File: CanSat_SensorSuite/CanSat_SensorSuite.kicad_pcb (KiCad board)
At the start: 4 copper layers, 53 parts, among them J12 Molex_01x02, J13 Conn_02x03_Odd_Even, J2 USBC_Conn, J3 Micro_SD_Card, J4 Pin_01x02, U1 RP2350_80QFN, U2 S25FL128, U3 NCP1117_3.3, X1 ABM8-272-T3

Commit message: Example files update
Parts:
- removed BUZ1: ~, 0_Passives:BUZZER,7.5x7.5mm
- removed C19: 100nF, 0_Capacitors:C_0603_1608_DensityHigh
- removed D1: ~, 0_Passives:LED_0805_2012Metric
- removed J12: Molex_01x02, 0_Connectors:502352_0201
- removed J3: Micro_SD_Card, 0_Connectors:Molex_472192001_uSD
- removed LED1: Green, 0_Passives:LED_0603_1608Metric
- removed LED2: Red, 0_Passives:LED_0603_1608Metric
- removed R10, R9: 4k7R, 0_Resistors:R_0603_1608_DensityHigh
- removed R7, R8: ?220R?, 0_Resistors:R_0603_1608_DensityHigh
- moved C5 15.0 mm to (121.5, 90.4)
- moved C6 15.0 mm to (126.8, 95.5)
- moved C1 15.0 mm to (134.8, 81.7)
- moved C10 15.0 mm to (137.0, 83.9)
- moved C11 15.0 mm to (128.1, 79.0)
- moved C12 15.0 mm to (124.5, 81.5)
- moved C13 15.0 mm to (120.6, 88.0)
- moved C14 15.0 mm to (137.5, 87.7)
- moved C15 15.0 mm to (130.9, 96.5)
- moved C16 15.0 mm to (128.1, 98.6)
- moved C17 15.0 mm to (131.1, 98.6)
- moved C18 15.0 mm to (132.4, 72.4)
- moved C2 15.0 mm to (132.5, 82.1)
- moved C20 15.0 mm to (170.3, 61.7)
- moved C21 15.0 mm to (170.3, 64.1)
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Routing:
- net /CCT Board Schematic/MCU & Peripherals/STATUS_BUZZER-: track 8.23 -> 0.00 mm
- net /CCT Board Schematic/MCU & Peripherals/STATUS_BUZZER+: track 6.72 -> 0.00 mm
- net /CCT Board Schematic/MCU & Peripherals/STATUS_LED_R: track 4.68 -> 0.00 mm
- net +3V3: track 40.2 -> 37.6 mm, vias 5 -> 4
- net /CCT Board Schematic/MCU & Peripherals/STATUS_LED_G: track 2.34 -> 0.00 mm
- net Net-(LED2-K): track 1.56 -> 0.00 mm
- net Net-(LED1-K): track 1.56 -> 0.00 mm
- net GND: vias 29 -> 28
- added copper zone on In2.Cu, net +3V3
- added copper zone on B.Cu, net GND
- added copper zone on In1.Cu, net GND
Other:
- board outline added: 100 x 80 mm
- board text removed: "???mm"
- board text removed: "???mm (?oz)"
- board text removed: "B.Mask"
- board text removed: "B.Paste"
- board text removed: "B.Silkscreen"
- board text removed: "Copper"
- board text removed: "Core"
- board text removed: "Dielectric"
- board text removed: "Dielectric Material"
- board text removed: "F.Mask"
- board text removed: "F.Paste"
- board text removed: "F.Silkscreen"
- board text removed: "FABRICATION NOTES (UNLESS OTHERWISE SPECIFIED) 1) OUTLINE DEFINED IN SEPARATE GERBER FILE WITH {dblquote}Edge_Cuts.GBR{dblquote} SUFFIX. DIMENSIONS OF CIRCUMSIZED RECTANGLE SHOWN ON THIS DWG FOR REF ONLY. 2) SEE SEPARATE DRILL FILES WITH {dblquote}.DRL{dblquote} SUFFIX FOR HOLE LOCATIONS. SELECTED HOLE LOCATIONS SHOWN ON THIS DWG FOR REF ONLY. 3) IMPEDANCE CONTROL REQUIRED. Microstrip 100-Ohm Dif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"
- board text removed: "FR-4"
- board text removed: "GBR"
- board text removed: "Gerber"
- board text removed: "Internal Plane"
- board text removed: "L1 (Sig, PWR)"
- board text removed: "L2 (GND)"
- board text removed: "L3 (Sig, PWR)"
- board text removed: "L4 (Sig, PWR)"
- board text removed: "L5 (GND)"
- board text removed: "L6 (Sig, PWR)"
- board text removed: "Layer"
- board text removed: "Layer Stack Legend"
- board text removed: "Legend"
- board text removed: "Material"
- board text removed: "Note: external layer thicknesses are specified after plating."
- board text removed: "Paste Mask"
- board text removed: "Prepreg"
- board text removed: "Signal"
- board text removed: "Solder Mask"
- board text removed: "Solder Resist"
- board text removed: "Thickness"
- board text removed: "Total thickness: 1.62mm"

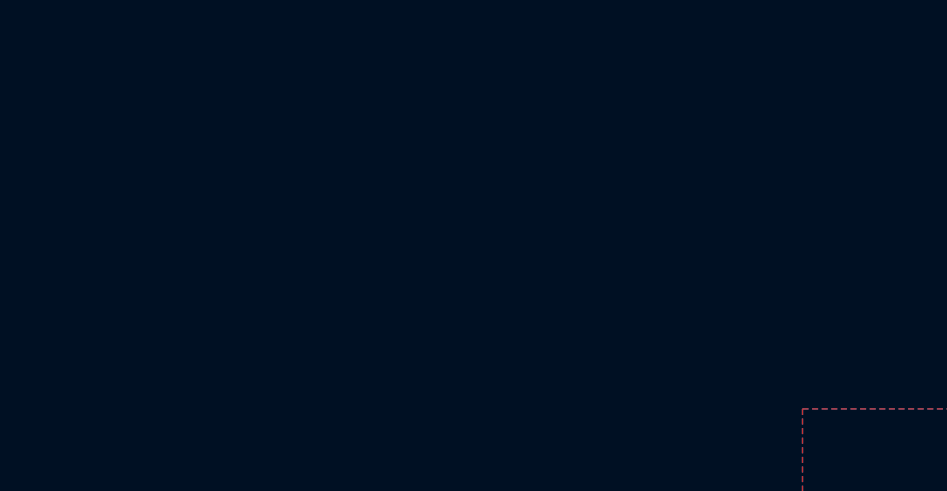
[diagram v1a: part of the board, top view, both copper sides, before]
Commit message: Minor schematic changes
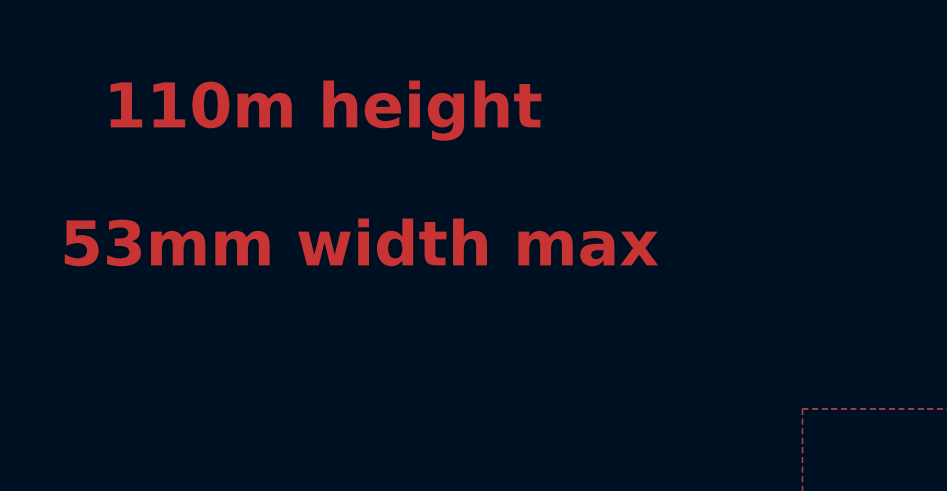
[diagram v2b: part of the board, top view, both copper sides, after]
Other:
- board text added: "110m height"
- board text added: "53mm width max"
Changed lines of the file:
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@@
 		(layer "User.9")
+	)
+	(gr_text "110m height\n"
+		(at 74.2 38.3 0)
+		(layer "F.Cu")
+		(effects
+			(font
+				(size 1.5 1.5)
+				(thickness 0.3)
+				(bold yes)
+			)
+			(justify left bottom)
+		)
+	)
+	(gr_text "53mm width max\n"
+		(at 72.75 42.9 0)
+		(layer "F.Cu")
+		(effects
+			(font
+				(size 1.5 1.5)
+				(thickness 0.3)
+				(bold yes)
+			)
+			(justify left bottom)
+		)
 	)
 	(gr_text "Top View"

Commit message: Major sensor suite board changes, start of PCB layout
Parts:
- removed J13: Conn_02x03_Odd_Even, 0_Connectors:PinHeader_2x03_P1.27mm_Vertical
- added BUZ1: ~, 0_Passives:BUZZER,5x5mm, F.Cu at (175.0, 99.3)
- added C101: 100nF, 0_Capacitors:C_0603_1608_DensityHigh, F.Cu at (170.8, 121.7)
- added C102: 100nF, 0_Capacitors:C_0603_1608_DensityHigh, F.Cu at (165.1, 123.0)
- added C103: 100nF, 0_Capacitors:C_0603_1608_DensityHigh, F.Cu at (148.1, 123.4)
- added C19: 100nF, 0_Capacitors:C_0603_1608_DensityHigh, F.Cu at (139.0, 100.3)
- added C201: 100nF, 0_Capacitors:C_0603_1608_DensityHigh, F.Cu at (155.7, 104.6)
- added C202: 100nF, 0_Capacitors:C_0603_1608_DensityHigh, F.Cu at (151.6, 116.1)
- added C24: 10uF, 0_Capacitors:C_0603_1608_DensityHigh, F.Cu at (153.4, 75.4)
- added C25: 10uF, 0_Capacitors:C_0603_1608_DensityHigh, F.Cu at (151.2, 75.4)
- added D1: ~, 0_Passives:D_SOD-323, F.Cu at (175.2, 94.7)
- added F3: Fuse, 0_Power:Fuse_1210_3225Metric, F.Cu at (162.6, 68.6)
- added FID301: Fiducial Marker, 0_Mechanical:Fiducial_1mm_Mask2mm, F.Cu at (134.3, 134.6)
- added FID302: Fiducial Marker, 0_Mechanical:Fiducial_1mm_Mask2mm, F.Cu at (175.3, 133.0)
- added FID303: Fiducial Marker, 0_Mechanical:Fiducial_1mm_Mask2mm, F.Cu at (142.1, 39.3)
- added G***: LOGO, SUSF_Footprint_Lib:SUSF_LOGO_BIG, F.Cu at (154.4, 134.8)
- added J1: Micro_SD_Card, 0_Connectors:Molex_472192001_uSD, F.Cu at (137.7, 109.8)
- added J101: SPS30, 0_Connectors:JST-S5B-ZR, F.Cu at (174.8, 127.6)
- added J104: Molex_01x02, 0_Connectors:502352_0201, F.Cu at (173.9, 112.0)
- added J3: USBC_Conn, 0_Connectors:USB4105_GCT, F.Cu at (155.0, 39.3)
- added J401: Molex_01x02, 0_Connectors:502352_0201, F.Cu at (136.1, 126.9)
- added J402: Conn_02x03, 0_Connectors:PinHeader_2x03_P1.27mm_Vertical, F.Cu at (167.5, 91.3)
- added LED1: Green, 0_Passives:LED_0603_1608Metric, F.Cu at (176.7, 88.2)
- added LED2: Red, 0_Passives:LED_0603_1608Metric, F.Cu at (176.7, 90.8)
- added LED3: Red, 0_Passives:LED_0603_1608Metric, F.Cu at (143.0, 47.6)
- added LED4: Red, 0_Passives:LED_0603_1608Metric, F.Cu at (151.9, 59.4)
- added LED5: Red, 0_Passives:LED_0603_1608Metric, F.Cu at (148.7, 75.7)
- added MH301: M3_MountingHole_Pad, 0_Mechanical:MountingHole_3.2mm_M3_Pad_Via, F.Cu at (135.0, 140.0)
- added MH302: M3_MountingHole_Pad, 0_Mechanical:MountingHole_3.2mm_M3_Pad_Via, F.Cu at (175.0, 140.0)
- added MH303: M3_MountingHole_Pad, 0_Mechanical:MountingHole_3.2mm_M3_Pad_Via, F.Cu at (135.0, 40.0)
- added MH304: M3_MountingHole_Pad, 0_Mechanical:MountingHole_3.2mm_M3_Pad_Via, F.Cu at (175.0, 40.0)
- added R10: 4.7kR, 0_Resistors:R_0603_1608_DensityHigh, F.Cu at (152.9, 100.9)
- added R14: 51R, 0_Resistors:R_0603_1608_DensityHigh, F.Cu at (152.1, 63.0)
- added R15: ???R, 0_Resistors:R_0603_1608_DensityHigh, F.Cu at (159.9, 75.2)
- added R16: ???R, 0_Resistors:R_0603_1608_DensityHigh, F.Cu at (157.8, 75.2)
- added R17: 51R, 0_Resistors:R_0603_1608_DensityHigh, F.Cu at (155.6, 75.2)
- added R18: 470kR, 0_Resistors:R_0603_1608_DensityHigh, F.Cu at (162.8, 76.3)
- added R19: 390kR, 0_Resistors:R_0603_1608_DensityHigh, F.Cu at (162.8, 78.5)
- added R7: 51R, 0_Resistors:R_0603_1608_DensityHigh, F.Cu at (173.7, 88.4)
- added R8: 51R, 0_Resistors:R_0603_1608_DensityHigh, F.Cu at (173.7, 90.5)
- added R9: 4.7kR, 0_Resistors:R_0603_1608_DensityHigh, F.Cu at (152.9, 98.8)
- added S1: SPST_1101M2S3AQE2, 0_Power:1101M2S3AQE2, F.Cu at (166.9, 69.2)
- added U102: ZMOD4410AI1R, 0_Sensors:ZMOD4410AI1R, F.Cu at (165.3, 127.0)
- added U103: STC31-C-R3, 0_Sensors:STC31-C-R3, F.Cu at (147.4, 128.6)
- added U201: MS560702BA03-50, 0_Sensors:MS5607-02BA03, F.Cu at (155.1, 107.3)
- added U202: LSM6DSOQTR, 0_Sensors:LSM6DSOQTR, F.Cu at (154.7, 115.9)
- added U4: NCP1117_3.3, 0_Power:SOT-223-3_TabPin2, F.Cu at (157.3, 58.8)
- added U5: MIC29302AWD, 0_Power:MIC29302AWD, F.Cu at (157.0, 69.0)
- C20, C21: value DNP -> 10nF
- F1, F2: footprint 0_Passives:Fuse_2512_6332Metric -> 0_Power:Fuse_1210_3225Metric
- J2: value USBC_Conn -> Pin_01x02; footprint 0_Connectors:USB4105_GCT -> 0_Connectors:PinHeader_1x02_P2.54mm_Vertical
- J4: value Pin_01x02 -> XT30_THT_H; footprint 0_Connectors:PinHeader_1x02_P2.54mm_Vertical -> 0_Connectors:XT30_THT_H
- L1: value 1uH -> 3.3uH
- R1, R2, R6: footprint 0_Resistors:R_0402_1005_DensityHigh -> 0_Resistors:R_0603_1608_DensityHigh
- R13: value 0R -> 51R; footprint 0_Resistors:R_0805_2012_DensityHigh -> 0_Resistors:R_0603_1608_DensityHigh
- R4: value 10kR -> 1kR; footprint 0_Resistors:R_0603_1608_DensityHigh -> 0_Resistors:R_0402_1005_DensityMedium
- R5: value 1kR -> 10kR
- U1: value RP2350_80QFN -> RP2350B
- moved J2 46.5 mm to (134.8, 94.3), turned to 90 degrees
- moved R4 40.9 mm to (160.9, 95.7), turned to -45 degrees
- moved X1 35.6 mm to (165.0, 99.8), turned to 45 degrees
- moved U3 35.2 mm to (136.2, 54.3)
- moved F1 33.6 mm to (138.6, 47.2)
- moved C16 33.2 mm to (161.3, 98.4), turned to -135 degrees
- moved C17 32.3 mm to (163.3, 96.4), turned to 45 degrees
- moved J4 32.0 mm to (166.8, 54.7), turned to -90 degrees
- moved C15 32.0 mm to (160.3, 84.0), turned to -135 degrees
- moved C6 31.5 mm to (158.3, 97.1), turned to -45 degrees
- moved C7 31.1 mm to (159.2, 96.2), turned to -45 degrees
- moved R13 30.5 mm to (146.6, 48.0), turned to 180 degrees
- moved C21 30.4 mm to (143.3, 50.0), turned to 180 degrees
- moved C5 30.1 mm to (150.8, 97.3), turned to -135 degrees
- moved C13 29.1 mm to (148.6, 96.2), turned to 45 degrees
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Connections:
- net /CCT Board Schematic/MCU & Peripherals/QSPI_SCLK renamed /Sensor Board Schematic/MCU & Peripherals/QSPI_SCLK
- net /CCT Board Schematic/MCU & Peripherals/QSPI_SD0 renamed /Sensor Board Schematic/MCU & Peripherals/QSPI_SD0
- net /CCT Board Schematic/MCU & Peripherals/QSPI_SD1 renamed /Sensor Board Schematic/MCU & Peripherals/QSPI_SD1
- net /CCT Board Schematic/MCU & Peripherals/QSPI_SD2 renamed /Sensor Board Schematic/MCU & Peripherals/QSPI_SD2
- net /CCT Board Schematic/MCU & Peripherals/QSPI_SD3 renamed /Sensor Board Schematic/MCU & Peripherals/QSPI_SD3
- net /CCT Board Schematic/MCU & Peripherals/USB_DM renamed /Sensor Board Schematic/MCU & Peripherals/USB_DM
- net /CCT Board Schematic/MCU & Peripherals/USB_DP renamed /Sensor Board Schematic/MCU & Peripherals/USB_DP
- net /CCT Board Schematic/MCU & Peripherals/VREG_AVDD renamed /Sensor Board Schematic/MCU & Peripherals/VREG_AVDD
- net /CCT Board Schematic/MCU & Peripherals/VREG_LX renamed /Sensor Board Schematic/MCU & Peripherals/VREG_LX
- net /CCT Board Schematic/MCU & Peripherals/XIN renamed /Sensor Board Schematic/MCU & Peripherals/XIN
- C21 pad 1: GND -> +3V3
- C21 pad 2: VBUS_F -> GND
- C22 pad 2: VBUS_F -> VREG
- C23 pad 1: Net-(U3-VO) -> +3V3
- D2 pad 1: /CCT Board Schematic/USBC/D- -> /Sensor Board Schematic/USBC & Battery Supply/D-
- D2 pad 3: /CCT Board Schematic/USBC/D+ -> /Sensor Board Schematic/USBC & Battery Supply/D+
- D2 pad 4: /CCT Board Schematic/USBC/USB_D+ -> /Sensor Board Schematic/MCU & Peripherals/USB_D+
- D2 pad 6: /CCT Board Schematic/USBC/USB_D- -> /Sensor Board Schematic/MCU & Peripherals/USB_D-
- F1 pad 2: /CCT Board Schematic/USBC/VBUS_PF -> /Sensor Board Schematic/USBC & Battery Supply/VBUS_PF
- F2 pad 1: +3V3 -> /Sensor Board Schematic/USBC & Battery Supply/BAT_CONN_OUT
- F2 pad 2: Net-(U3-VO) -> VBUS
- J4 pad 1: /CCT Board Schematic/MCU & Peripherals/~{USB_BOOT} -> /Sensor Board Schematic/USBC & Battery Supply/BAT_CONN_IN
- R1 pad 1: /CCT Board Schematic/MCU & Peripherals/USB_D+ -> /Sensor Board Schematic/MCU & Peripherals/USB_D+
- R11 pad 2: /CCT Board Schematic/USBC/CC2 -> /Sensor Board Schematic/USBC & Battery Supply/CC2
- R12 pad 1: /CCT Board Schematic/USBC/CC1 -> /Sensor Board Schematic/USBC & Battery Supply/CC1
- R13 pad 1: VBUS -> GND
- R13 pad 2: VBUS_F -> Net-(LED3-K)
- R2 pad 1: /CCT Board Schematic/MCU & Peripherals/USB_D- -> /Sensor Board Schematic/MCU & Peripherals/USB_D-
- R4 pad 1: /CCT Board Schematic/MCU & Peripherals/QSPI_CS -> /Sensor Board Schematic/MCU & Peripherals/XOUT
- R4 pad 2: +3V3 -> Net-(C17-Pad1)
- R5 pad 1: /CCT Board Schematic/MCU & Peripherals/QSPI_CS -> /Sensor Board Schematic/MCU & Peripherals/QSPI_CS
- R5 pad 2: /CCT Board Schematic/MCU & Peripherals/~{USB_BOOT} -> +3V3
- R6 pad 1: /CCT Board Schematic/MCU & Peripherals/XOUT -> /Sensor Board Schematic/MCU & Peripherals/QSPI_CS
- R6 pad 2: Net-(C17-Pad1) -> /Sensor Board Schematic/MCU & Peripherals/~{USB_BOOT}
- U1 pad 1: /CCT Board Schematic/MCU & Peripherals/FIRE_SIGNAL -> /Sensor Board Schematic/MCU & Peripherals/SD_DAT1
- U1 pad 11: /CCT Board Schematic/MCU & Peripherals/Servo2_PWM -> unconnected-(U1A-GPIO12-Pad11)
- U1 pad 12: /CCT Board Schematic/MCU & Peripherals/SD_DAT1 -> unconnected-(U1A-GPIO13-Pad12)
- U1 pad 13: /CCT Board Schematic/MCU & Peripherals/Servo3_PWM -> unconnected-(U1A-GPIO14-Pad13)
- U1 pad 14: /CCT Board Schematic/MCU & Peripherals/SD_DAT0 -> unconnected-(U1A-GPIO15-Pad14)
- U1 pad 16: /CCT Board Schematic/MCU & Peripherals/SD_CLK -> unconnected-(U1A-GPIO16-Pad16)
- U1 pad 17: /CCT Board Schematic/MCU & Peripherals/SD_CMD -> unconnected-(U1A-GPIO17-Pad17)
- U1 pad 18: /CCT Board Schematic/MCU & Peripherals/SD_DAT3 -> unconnected-(U1A-GPIO18-Pad18)
- U1 pad 19: /CCT Board Schematic/MCU & Peripherals/SD_DAT2 -> unconnected-(U1A-GPIO19-Pad19)
- U1 pad 2: /CCT Board Schematic/MCU & Peripherals/ARM_SIGNAL -> /Sensor Board Schematic/MCU & Peripherals/SD_DAT0
- U1 pad 20: /CCT Board Schematic/MCU & Peripherals/I2C_SDA -> /Sensor Board Schematic/AtmoSensors/I2C_SDA
- U1 pad 21: /CCT Board Schematic/MCU & Peripherals/I2C_SCL -> /Sensor Board Schematic/AtmoSensors/I2C_SCL
- U1 pad 3: /CCT Board Schematic/MCU & Peripherals/FILL_SIGNAL -> /Sensor Board Schematic/MCU & Peripherals/SD_CLK
- U1 pad 31: /CCT Board Schematic/MCU & Peripherals/XOUT -> /Sensor Board Schematic/MCU & Peripherals/XOUT
- U1 pad 35: /CCT Board Schematic/MCU & Peripherals/RUN -> /Sensor Board Schematic/MCU & Peripherals/RUN
- U1 pad 38: /CCT Board Schematic/MCU & Peripherals/GPIO30 -> /Sensor Board Schematic/MCU & Peripherals/GPIO30
- U1 pad 39: /CCT Board Schematic/MCU & Peripherals/GPIO31 -> /Sensor Board Schematic/MCU & Peripherals/GPIO31
- U1 pad 4: /CCT Board Schematic/MCU & Peripherals/RJ45_LED2 -> /Sensor Board Schematic/MCU & Peripherals/SD_CMD
- U1 pad 40: /CCT Board Schematic/MCU & Peripherals/GPIO32 -> /Sensor Board Schematic/MCU & Peripherals/GPIO32
- U1 pad 44: /CCT Board Schematic/MCU & Peripherals/STATUS_BUZZER- -> /Sensor Board Schematic/MCU & Peripherals/STATUS_BUZZER-
- U1 pad 45: /CCT Board Schematic/MCU & Peripherals/STATUS_BUZZER+ -> /Sensor Board Schematic/MCU & Peripherals/STATUS_BUZZER+
- U1 pad 47: /CCT Board Schematic/MCU & Peripherals/STATUS_LED_R -> /Sensor Board Schematic/MCU & Peripherals/STATUS_LED_R
- U1 pad 48: /CCT Board Schematic/MCU & Peripherals/STATUS_LED_G -> /Sensor Board Schematic/MCU & Peripherals/STATUS_LED_G
- U1 pad 54: /CCT Board Schematic/MCU & Peripherals/PYRO_SENSE -> unconnected-(U1A-GPIO43_ADC3-Pad54)
- U1 pad 55: /CCT Board Schematic/MCU & Peripherals/PYRO_IN -> unconnected-(U1A-GPIO44_ADC4-Pad55)
- U1 pad 56: /CCT Board Schematic/MCU & Peripherals/PYRO_SEN -> unconnected-(U1A-GPIO45_ADC5-Pad56)
- U1 pad 58: /CCT Board Schematic/VBAT_sense -> /Sensor Board Schematic/MCU & Peripherals/VBAT_sense
- U1 pad 6: /CCT Board Schematic/MCU & Peripherals/RS485_TX -> /Sensor Board Schematic/MCU & Peripherals/SD_DAT3
- U1 pad 7: /CCT Board Schematic/MCU & Peripherals/RS485_RX -> /Sensor Board Schematic/MCU & Peripherals/SD_DAT2
- U1 pad 75: /CCT Board Schematic/MCU & Peripherals/QSPI_CS -> /Sensor Board Schematic/MCU & Peripherals/QSPI_CS
- U1 pad 8: /CCT Board Schematic/MCU & Peripherals/RJ45_LED1 -> unconnected-(U1A-GPIO10-Pad8)
- U1 pad 9: /CCT Board Schematic/MCU & Peripherals/Servo1_PWM -> unconnected-(U1A-GPIO11-Pad9)
- U2 pad 1: /CCT Board Schematic/MCU & Peripherals/QSPI_CS -> /Sensor Board Schematic/MCU & Peripherals/QSPI_CS
- U3 pad 2: Net-(U3-VO) -> +3V3
- U3 pad 3: VBUS_F -> VBUS
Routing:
- net /CCT Board Schematic/MCU & Peripherals/QSPI_CS: track 27.2 -> 0.00 mm, vias 2 -> 0
- net VBUS: track 21.9 -> 3.26 mm, vias 2 -> 1
- net /Sensor Board Schematic/MCU & Peripherals/QSPI_SD1: track 21.5 -> 5.17 mm, vias 2 -> 0
- net /Sensor Board Schematic/MCU & Peripherals/QSPI_SD2: track 19.6 -> 5.06 mm
- net /Sensor Board Schematic/USBC & Battery Supply/VBUS_PF: track 0.00 -> 12.2 mm
- net /CCT Board Schematic/USBC/VBUS_PF: track 12.2 -> 0.00 mm
- net /Sensor Board Schematic/MCU & Peripherals/RUN: track 0.00 -> 10.3 mm
- net /CCT Board Schematic/MCU & Peripherals/RUN: track 10.3 -> 0.00 mm
- net VBUS_F: track 8.85 -> 0.00 mm
- net /CCT Board Schematic/MCU & Peripherals/GPIO30: track 8.43 -> 0.00 mm
- net /Sensor Board Schematic/MCU & Peripherals/GPIO30: track 0.00 -> 8.43 mm
- net /Sensor Board Schematic/MCU & Peripherals/QSPI_SD3: track 11.4 -> 4.14 mm
- net /Sensor Board Schematic/MCU & Peripherals/GPIO32: track 0.00 -> 7.08 mm
- net /CCT Board Schematic/MCU & Peripherals/GPIO32: track 7.08 -> 0.00 mm
- net /Sensor Board Schematic/MCU & Peripherals/QSPI_SD0: track 11.3 -> 4.37 mm
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- added copper zone on F.Cu, net (none)
- removed copper zone on F.Cu, net /Sensor Board Schematic/MCU & Peripherals/VREG_LX
- removed copper zone on F.Cu, net Net-(U3-VO)
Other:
- board size 100 x 80 mm -> 50 x 110 mm
- board text removed: "??? ??? ???"
- board text removed: "??? ??? ??? ??? ??? (slot) ??? ??? ??? ??? ???"
- board text removed: "???mm ???mm ???mm ???mm ???mm ???mm ???mm ???mm ???mm ???mm"
- board text removed: "ASSEMBLY NOTES (UNLESS OTHERWISE SPECIFIED) 1) DO NOT POPULATE PARTS ARE MARKED WITH A RED CROSS. 2) DO NOT POPULATE PARTS ARE NOT PRESENT IN THE BOM. 3) IF CONFLICTING INFORMATION IS FOUND BETWEEN THE ASSEMBLY FILE AND BOM, BOM SHOULD BE USED AS THE MAIN SOURCE."
- board text removed: "Back Side"
- board text removed: "Bottom Assembly (Scale 1:1)"
- board text removed: "Bottom Test Points (Scale 1:1)"
- board text removed: "Bottom View"
- board text removed: "Components"
- board text removed: "Count"
- board text removed: "Drill Drawing (Top View) (Scale 1:1)"
- board text removed: "Front Side"
- board text removed: "Hole Size"
- board text removed: "Net"
- board text removed: "Plated"
- board text removed: "Plated Plated Plated Plated Plated Plated Plated Plated Plated Unplated"
- board text removed: "Ref."
- board text removed: "Symbol"
- board text removed: "THT SMD Total"
- board text removed: "TP? TP? TP?"
- board text removed: "Top Assembly (Scale 1:1)"
- board text removed: "Top Test Points (Scale 1:1)"
- board text removed: "Top View"
- board text removed: "Total"
- board text removed: "Type"
- board text removed: "X"
- board text removed: "X [mm]"
- board text removed: "Y"
- board text removed: "Y [mm]"

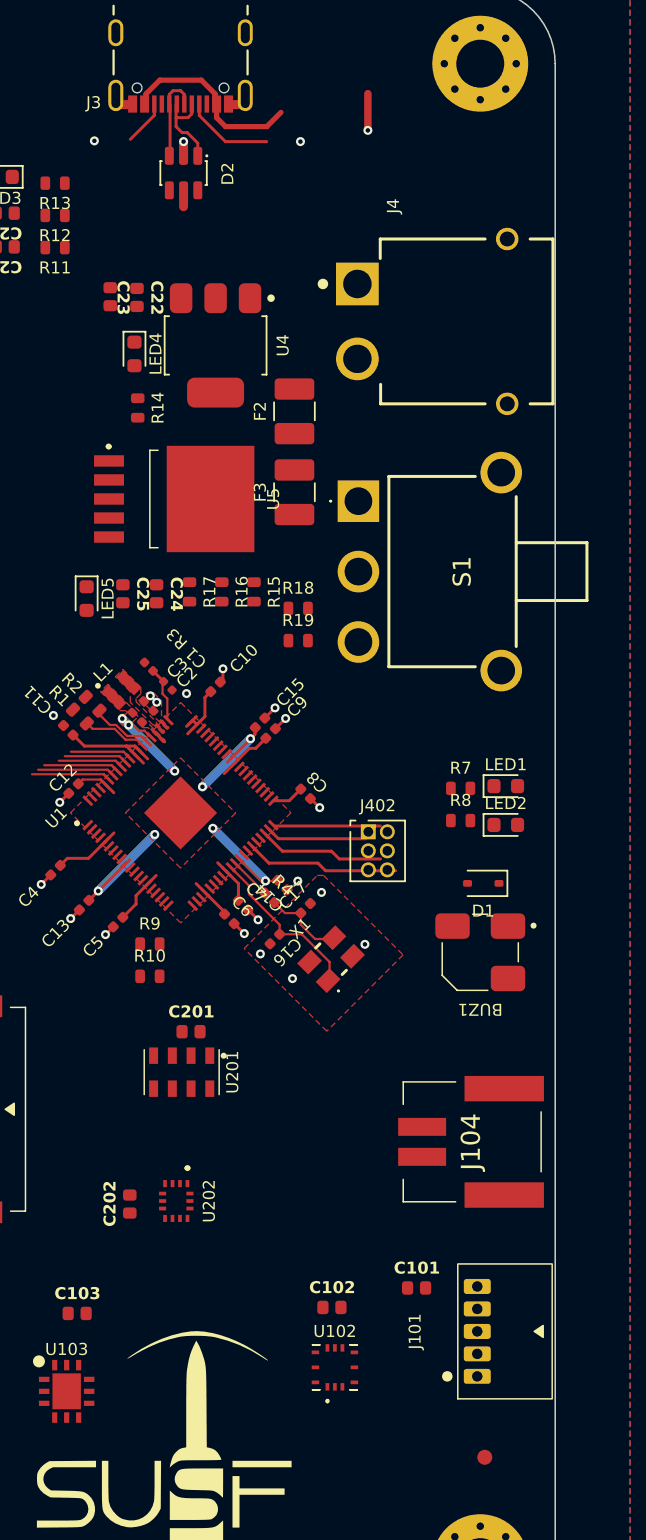
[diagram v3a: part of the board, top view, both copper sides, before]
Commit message: Minor schematic adjustments
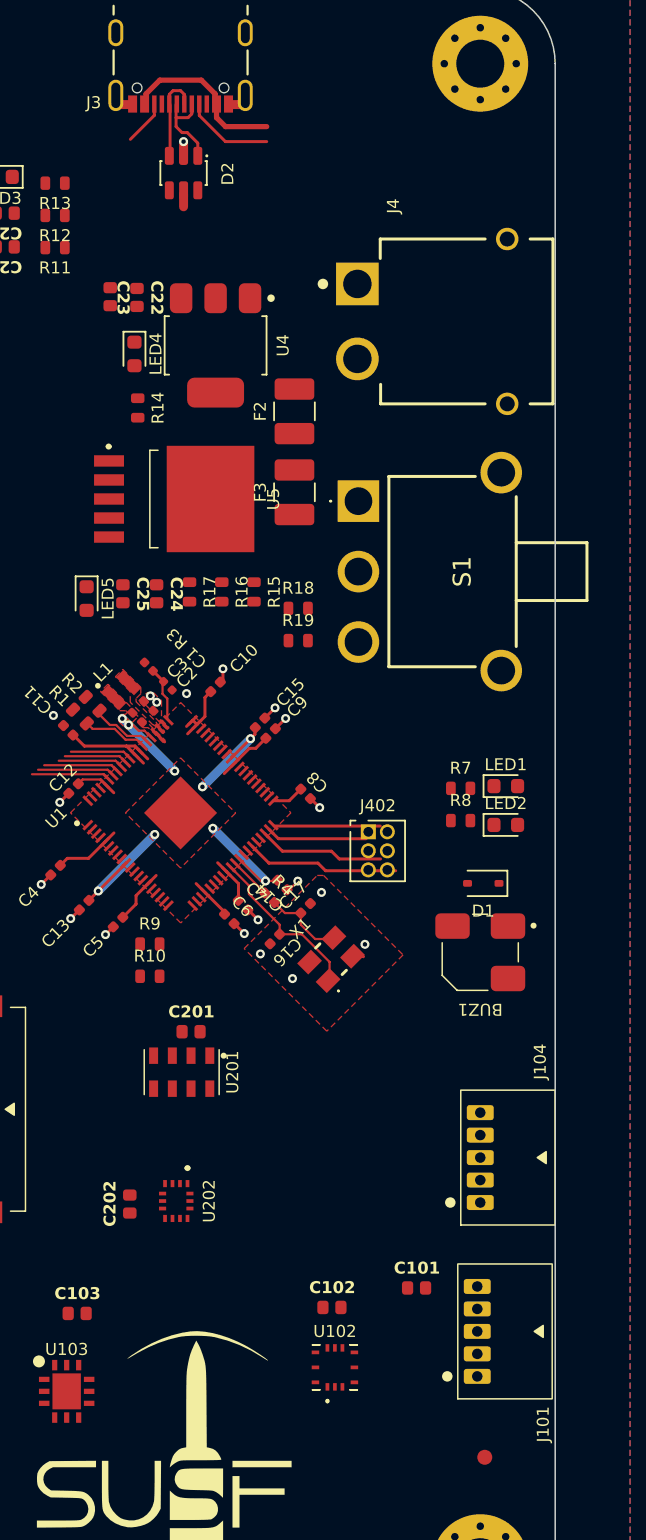
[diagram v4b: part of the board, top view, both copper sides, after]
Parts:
- J104: value Molex_01x02 -> JST-S5B-ZR; footprint 0_Connectors:502352_0201 -> 0_Connectors:JST-S5B-ZR
- moved J104 4.21 mm to (175.0, 116.0)
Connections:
- J104 pad 1: /Sensor Board Schematic/AtmoSensors/I2C_SDA -> +3V3
- J104 pad 2: /Sensor Board Schematic/AtmoSensors/I2C_SCL -> unconnected-(J104-NC-Pad2)
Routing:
- net VBUS: track 3.26 -> 0.81 mm, vias 1 -> 0
- net /Sensor Board Schematic/USBC & Battery Supply/VBUS_PF: track 12.2 -> 10.9 mm
- net GND: track 12.6 -> 13.4 mm, vias 22 -> 20
